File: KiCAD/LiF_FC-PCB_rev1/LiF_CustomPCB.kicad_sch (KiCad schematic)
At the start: 0 parts

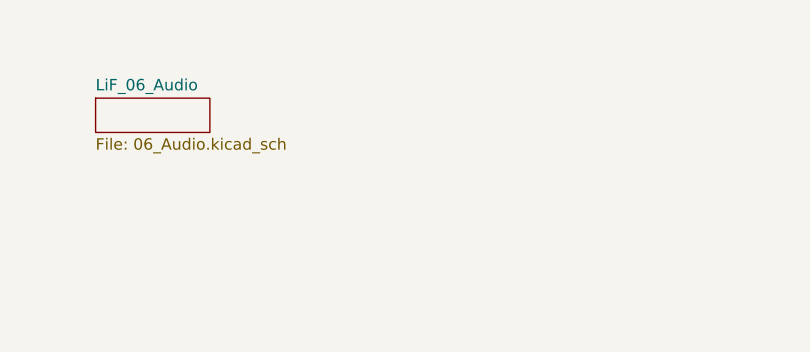
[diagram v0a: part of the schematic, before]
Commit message: fixed my schematics syncing (I think), and added accelorometer schematic. Pushing since I need to switch main.
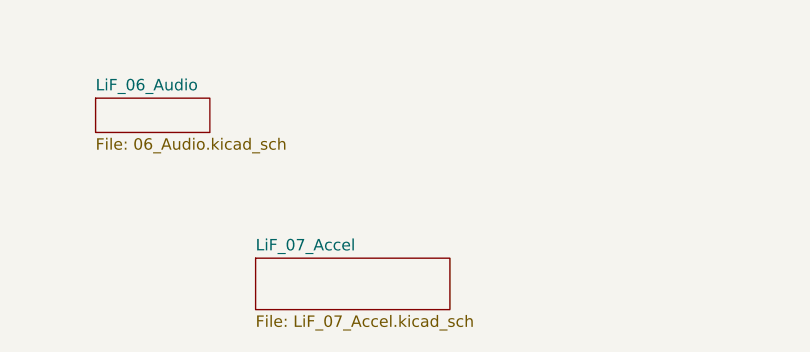
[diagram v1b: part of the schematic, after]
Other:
- added sheet LiF_07_Accel (LiF_07_Accel.kicad_sch)
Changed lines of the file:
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@@
+	)
+	(sheet
+		(at 107.95 145.415)
+		(size 21.59 5.715)
+		(exclude_from_sim no)
+		(in_bom yes)
+		(on_board yes)
+		(dnp no)
+		(fields_autoplaced yes)
+		(stroke
+			(width 0.1524)
+			(type solid)
+		)
+		(fill
+			(color 0 0 0 0.0000)
+		)
+		(property "Sheetname" "LiF_07_Accel"
+			(at 107.95 144.7034 0)
+			(effects
+				(font
+					(size 1.27 1.27)
+				)
+				(justify left bottom)
+			)
+		)
+		(property "Sheetfile" "LiF_07_Accel.kicad_sch"
+			(at 107.95 151.7146 0)
+			(effects
+				(font
+					(size 1.27 1.27)
+				)
+				(justify left top)
+			)
+		)
+		(property "Field2" ""
+			(at 107.95 145.415 0)
+			(effects
+				(font
+					(size 1.27 1.27)
+				)
+			)
+		)
+		(instances
+			(project "LiF_CustomPCB"
+				(path "/e8d53809-63ab-4a8d-88b7-d7504d15b103"
+					(page "8")
+				)
+			)
+		)
 	)
 	(sheet
